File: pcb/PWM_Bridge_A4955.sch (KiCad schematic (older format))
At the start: 18 parts, among them Q3 IPD079N06L3G, Q4 IPD079N06L3G, Q5 IPD079N06L3G, Q6 IPD079N06L3G, U5 A4955GLPTR-T

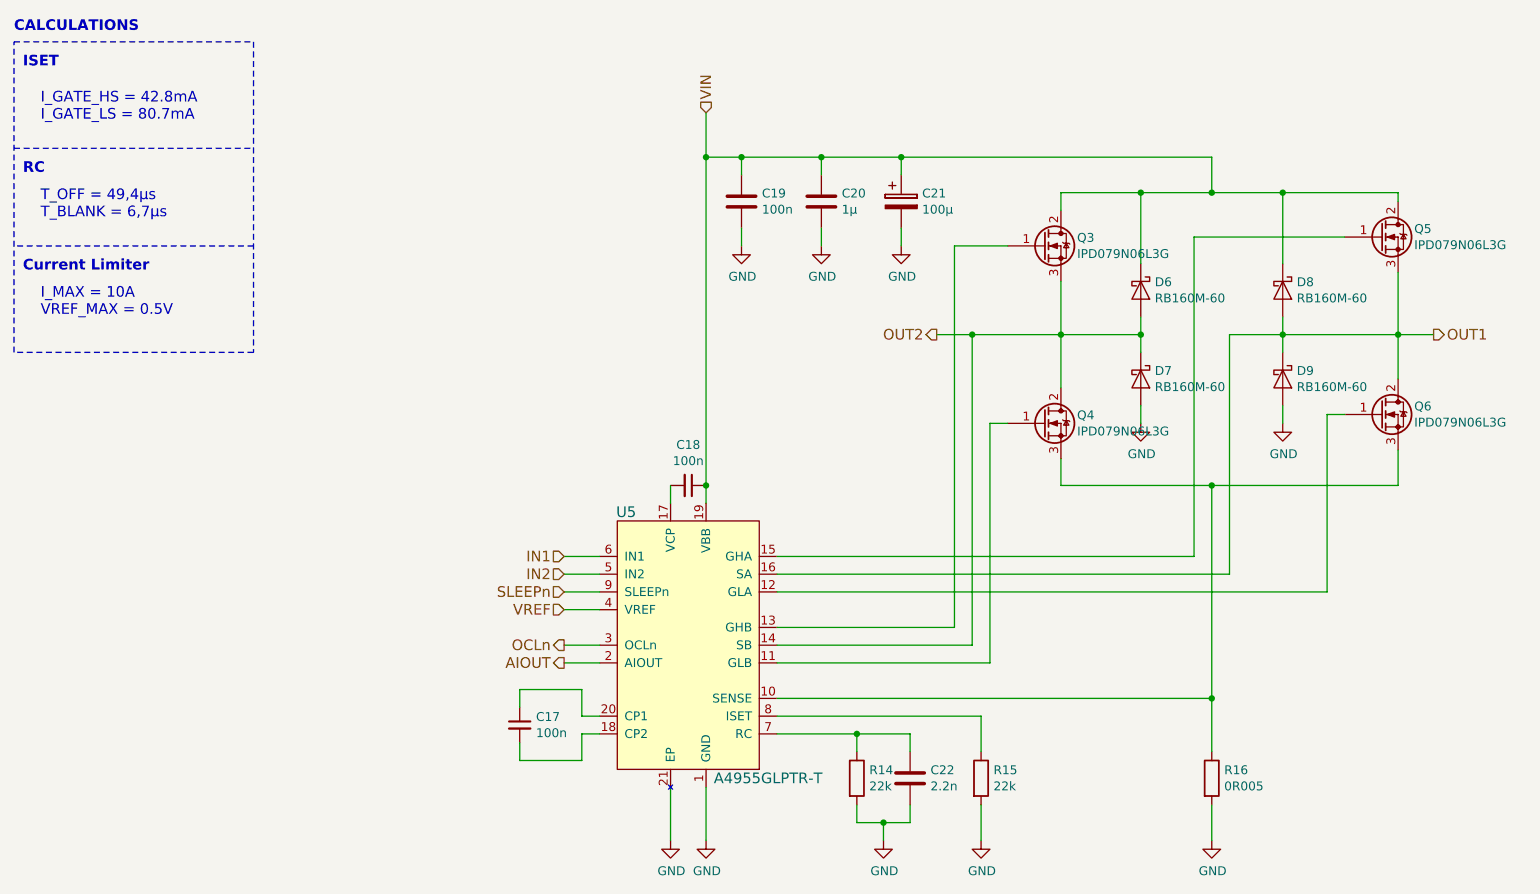
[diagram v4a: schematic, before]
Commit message: Fix schematic error described in #8
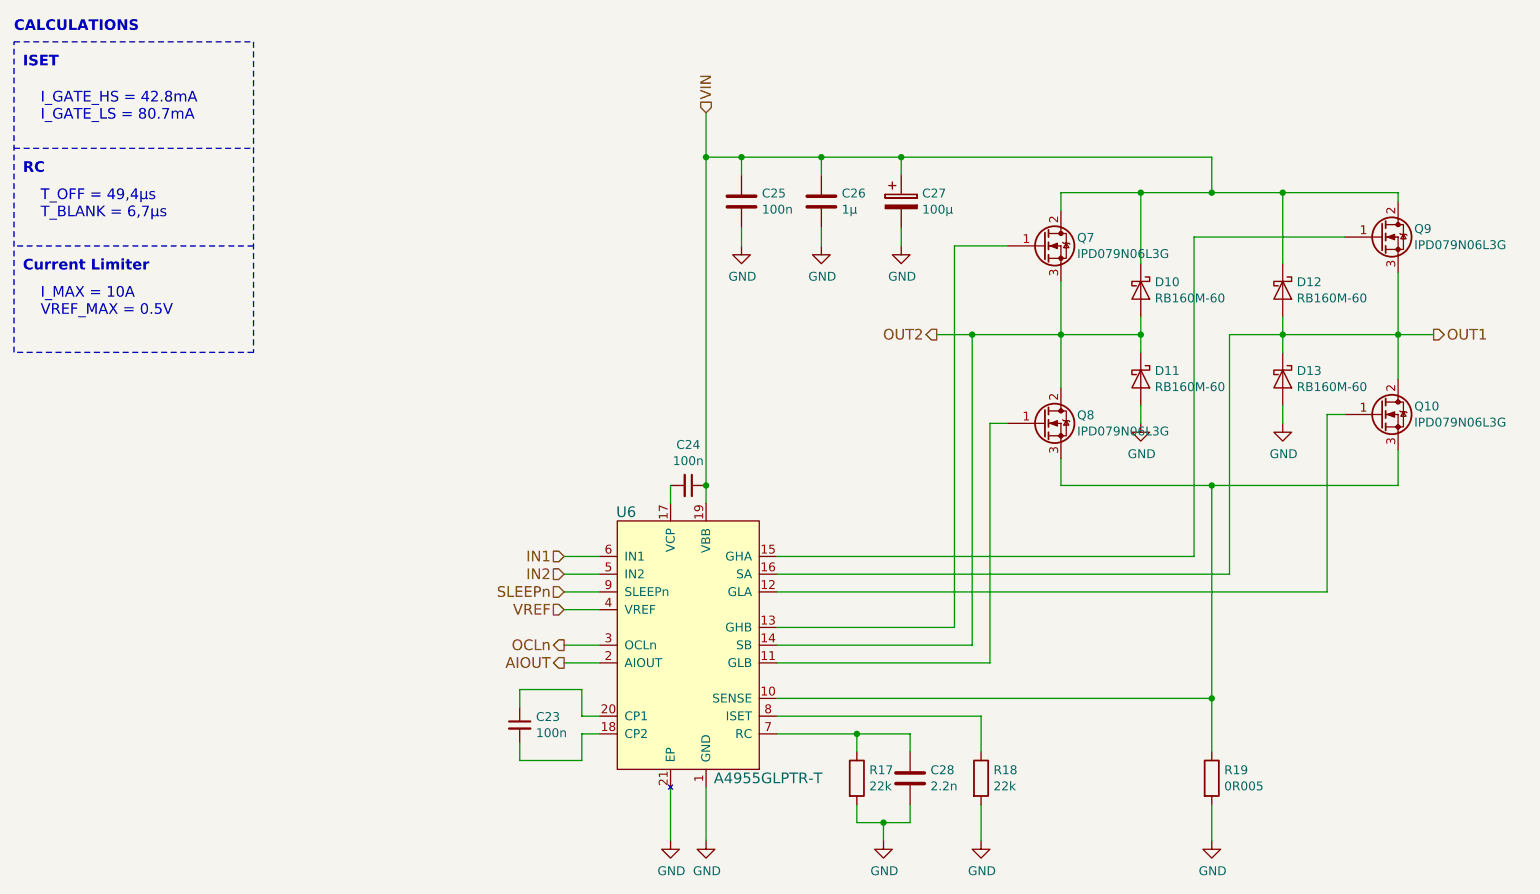
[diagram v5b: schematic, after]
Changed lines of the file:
@@
 $Descr A4 11693 8268
 encoding utf-8
-Sheet 3 7
+Sheet 4 7
 Title "A4955 PWM Bridge"
 Date "2016-12-03"
@@
 AR Path="/58077727/58077F1C" Ref="U5"  Part="1"
 AR Path="/58084D17/58077F1C" Ref="U6"  Part="1"
-F 0 "U5" H 4300 5150 60  0000 C CNN
+F 0 "U6" H 4300 5150 60  0000 C CNN
 F 1 "A4955GLPTR-T" H 5100 3650 60  0000 C CNN
 F 2 "Housings_SSOP:ETSSOP-20-1EP_4.4x6.5mm_Pitch0.65mm" H 4650 4400 60  0001 C CNN
@@
 AR Path="/58077727/5807829A" Ref="C18"  Part="1"
 AR Path="/58084D17/5807829A" Ref="C24"  Part="1"
-F 0 "C18" V 4421 3500 50  0000 C CNN
+F 0 "C24" V 4421 3500 50  0000 C CNN
 F 1 "100n" V 4512 3500 50  0000 C CNN
 F 2 "Capacitors_SMD:C_0603" H 4650 3500 50  0001 C CNN
@@
 AR Path="/58077727/58078520" Ref="R14"  Part="1"
 AR Path="/58084D17/58078520" Ref="R17"  Part="1"
-F 0 "R14" H 5670 5196 50  0000 L CNN
+F 0 "R17" H 5670 5196 50  0000 L CNN
 F 1 "22k" H 5670 5105 50  0000 L CNN
 F 2 "Resistors_SMD:R_0603" V 5530 5150 50  0001 C CNN
@@
 AR Path="/58077727/5807867B" Ref="C22"  Part="1"
 AR Path="/58084D17/5807867B" Ref="C28"  Part="1"
-F 0 "C22" H 6015 5196 50  0000 L CNN
+F 0 "C28" H 6015 5196 50  0000 L CNN
 F 1 "2.2n" H 6015 5105 50  0000 L CNN
 F 2 "Capacitors_SMD:C_0603" H 5938 5000 50  0001 C CNN
@@
 $EndComp
 $Comp
-L GND #PWR073
+L GND #PWR072
 U 1 1 580787DB
 P 5750 5500
-AR Path="/58077727/580787DB" Ref="#PWR073"  Part="1"
-AR Path="/58084D17/580787DB" Ref="#PWR083"  Part="1"
-F 0 "#PWR073" H 5750 5250 50  0001 C CNN
+AR Path="/58077727/580787DB" Ref="#PWR072"  Part="1"
+AR Path="/58084D17/580787DB" Ref="#PWR082"  Part="1"
+F 0 "#PWR082" H 5750 5250 50  0001 C CNN
 F 1 "GND" H 5755 5327 50  0000 C CNN
 F 2 "" H 5750 5500 50  0000 C CNN
@@
 $EndComp
 $Comp
-L GND #PWR074
+L GND #PWR073
 U 1 1 58078835
 P 4750 5500
-AR Path="/58077727/58078835" Ref="#PWR074"  Part="1"
-AR Path="/58084D17/58078835" Ref="#PWR084"  Part="1"
-F 0 "#PWR074" H 4750 5250 50  0001 C CNN
+AR Path="/58077727/58078835" Ref="#PWR073"  Part="1"
+AR Path="/58084D17/58078835" Ref="#PWR083"  Part="1"
+F 0 "#PWR083" H 4750 5250 50  0001 C CNN
 F 1 "GND" H 4755 5327 50  0000 C CNN
 F 2 "" H 4750 5500 50  0000 C CNN
@@
 AR Path="/58077727/580789CE" Ref="R16"  Part="1"
 AR Path="/58084D17/580789CE" Ref="R19"  Part="1"
-F 0 "R16" H 7670 5196 50  0000 L CNN
+F 0 "R19" H 7670 5196 50  0000 L CNN
 F 1 "0R005" H 7670 5105 50  0000 L CNN
 F 2 "Resistors_SMD:R_2512" V 7530 5150 50  0001 C CNN
@@
 $EndComp
 $Comp
-L GND #PWR075
+L GND #PWR074
 U 1 1 58078AB1
 P 7600 5500
-AR Path="/58077727/58078AB1" Ref="#PWR075"  Part="1"
-AR Path="/58084D17/58078AB1" Ref="#PWR085"  Part="1"
-F 0 "#PWR075" H 7600 5250 50  0001 C CNN
+AR Path="/58077727/58078AB1" Ref="#PWR074"  Part="1"
+AR Path="/58084D17/58078AB1" Ref="#PWR084"  Part="1"
+F 0 "#PWR084" H 7600 5250 50  0001 C CNN
 F 1 "GND" H 7605 5327 50  0000 C CNN
 F 2 "" H 7600 5500 50  0000 C CNN
@@
 AR Path="/58077727/58078C46" Ref="Q3"  Part="1"
 AR Path="/58084D17/58078C46" Ref="Q7"  Part="1"
-F 0 "Q3" H 6841 2196 50  0000 L CNN
+F 0 "Q7" H 6841 2196 50  0000 L CNN
 F 1 "IPD079N06L3G" H 6841 2105 50  0000 L CNN
 F 2 "TO_SOT_Packages_SMD_local:PG-TO-252-3-313" H 6850 2250 50  0001 C CNN
@@
 AR Path="/58077727/58078E80" Ref="Q5"  Part="1"
 AR Path="/58084D17/58078E80" Ref="Q9"  Part="1"
-F 0 "Q5" H 8741 2146 50  0000 L CNN
+F 0 "Q9" H 8741 2146 50  0000 L CNN
 F 1 "IPD079N06L3G" H 8741 2055 50  0000 L CNN
 F 2 "TO_SOT_Packages_SMD_local:PG-TO-252-3-313" H 8750 2200 50  0001 C CNN
@@
 AR Path="/58077727/58078ED9" Ref="Q6"  Part="1"
 AR Path="/58084D17/58078ED9" Ref="Q10"  Part="1"
-F 0 "Q6" H 8741 3146 50  0000 L CNN
+F 0 "Q10" H 8741 3146 50  0000 L CNN
 F 1 "IPD079N06L3G" H 8741 3055 50  0000 L CNN
 F 2 "TO_SOT_Packages_SMD_local:PG-TO-252-3-313" H 8750 3200 50  0001 C CNN
@@
 AR Path="/58077727/58078F3F" Ref="Q4"  Part="1"
 AR Path="/58084D17/58078F3F" Ref="Q8"  Part="1"
-F 0 "Q4" H 6841 3196 50  0000 L CNN
+F 0 "Q8" H 6841 3196 50  0000 L CNN
 F 1 "IPD079N06L3G" H 6841 3105 50  0000 L CNN
 F 2 "TO_SOT_Packages_SMD_local:PG-TO-252-3-313" H 6850 3250 50  0001 C CNN
@@
 AR Path="/58077727/5807A394" Ref="C19"  Part="1"
 AR Path="/58084D17/5807A394" Ref="C25"  Part="1"
-F 0 "C19" H 5065 1946 50  0000 L CNN
+F 0 "C25" H 5065 1946 50  0000 L CNN
 F 1 "100n" H 5065 1855 50  0000 L CNN
 F 2 "Capacitors_SMD:C_0603" H 4988 1750 50  0001 C CNN
@@
 $EndComp
 $Comp
-L GND #PWR076
+L GND #PWR075
 U 1 1 5807A4C6
 P 4950 2150
-AR Path="/58077727/5807A4C6" Ref="#PWR076"  Part="1"
-AR Path="/58084D17/5807A4C6" Ref="#PWR086"  Part="1"
-F 0 "#PWR076" H 4950 1900 50  0001 C CNN
+AR Path="/58077727/5807A4C6" Ref="#PWR075"  Part="1"
+AR Path="/58084D17/5807A4C6" Ref="#PWR085"  Part="1"
+F 0 "#PWR085" H 4950 1900 50  0001 C CNN
 F 1 "GND" H 4955 1977 50  0000 C CNN
 F 2 "" H 4950 2150 50  0000 C CNN
@@
 AR Path="/58077727/5807A62E" Ref="C21"  Part="1"
 AR Path="/58084D17/5807A62E" Ref="C27"  Part="1"
-F 0 "C21" H 5968 1946 50  0000 L CNN
+F 0 "C27" H 5968 1946 50  0000 L CNN
 F 1 "100µ" H 5968 1855 50  0000 L CNN
 F 2 "Capacitors_SMD:c_elec_10x10" H 5888 1750 50  0001 C CNN
@@
 $EndComp
 $Comp
-L GND #PWR077
+L GND #PWR076
 U 1 1 5807A964
 P 5850 2150
-AR Path="/58077727/5807A964" Ref="#PWR077"  Part="1"
-AR Path="/58084D17/5807A964" Ref="#PWR087"  Part="1"
-F 0 "#PWR077" H 5850 1900 50  0001 C CNN
+AR Path="/58077727/5807A964" Ref="#PWR076"  Part="1"
+AR Path="/58084D17/5807A964" Ref="#PWR086"  Part="1"
+F 0 "#PWR086" H 5850 1900 50  0001 C CNN
 F 1 "GND" H 5855 1977 50  0000 C CNN
 F 2 "" H 5850 2150 50  0000 C CNN
@@
 AR Path="/58077727/5807BEA4" Ref="C17"  Part="1"
 AR Path="/58084D17/5807BEA4" Ref="C23"  Part="1"
-F 0 "C17" H 3792 4896 50  0000 L CNN
+F 0 "C23" H 3792 4896 50  0000 L CNN
 F 1 "100n" H 3792 4805 50  0000 L CNN
 F 2 "Capacitors_SMD:C_0603" H 3700 4850 50  0001 C CNN
@@
 AR Path="/58077727/5809AC71" Ref="C20"  Part="1"
 AR Path="/58084D17/5809AC71" Ref="C26"  Part="1"
-F 0 "C20" H 5515 1946 50  0000 L CNN
+F 0 "C26" H 5515 1946 50  0000 L CNN
 F 1 "1µ" H 5515 1855 50  0000 L CNN
 F 2 "Capacitors_SMD:C_0603" H 5438 1750 50  0001 C CNN
@@
 $EndComp
 $Comp
-L GND #PWR088
+L GND #PWR087
 U 1 1 5809ACB6
 P 5400 2150
-AR Path="/58084D17/5809ACB6" Ref="#PWR088"  Part="1"
-AR Path="/58077727/5809ACB6" Ref="#PWR078"  Part="1"
-F 0 "#PWR078" H 5400 1900 50  0001 C CNN
+AR Path="/58084D17/5809ACB6" Ref="#PWR087"  Part="1"
+AR Path="/58077727/5809ACB6" Ref="#PWR077"  Part="1"
+F 0 "#PWR087" H 5400 1900 50  0001 C CNN
 F 1 "GND" H 5405 1977 50  0000 C CNN
 F 2 "" H 5400 2150 50  0000 C CNN
@@
 AR Path="/58077727/580A461C" Ref="R15"  Part="1"
 AR Path="/58084D17/580A461C" Ref="R18"  Part="1"
-F 0 "R15" H 6370 5196 50  0000 L CNN
+F 0 "R18" H 6370 5196 50  0000 L CNN
 F 1 "22k" H 6370 5105 50  0000 L CNN
 F 2 "Resistors_SMD:R_0603" V 6230 5150 50  0001 C CNN
@@
 $EndComp
 $Comp
-L GND #PWR079
+L GND #PWR078
 U 1 1 580A46B3
 P 6300 5500
-AR Path="/58077727/580A46B3" Ref="#PWR079"  Part="1"
-AR Path="/58084D17/580A46B3" Ref="#PWR089"  Part="1"
-F 0 "#PWR079" H 6300 5250 50  0001 C CNN
+AR Path="/58077727/580A46B3" Ref="#PWR078"  Part="1"
+AR Path="/58084D17/580A46B3" Ref="#PWR088"  Part="1"
+F 0 "#PWR088" H 6300 5250 50  0001 C CNN
 F 1 "GND" H 6305 5327 50  0000 C CNN
 F 2 "" H 6300 5500 50  0000 C CNN
@@
 $EndComp
 $Comp
-L GND #PWR080
+L GND #PWR079
 U 1 1 581550B7
 P 8000 3150
-AR Path="/58077727/581550B7" Ref="#PWR080"  Part="1"
-AR Path="/58084D17/581550B7" Ref="#PWR090"  Part="1"
-F 0 "#PWR080" H 8000 2900 50  0001 C CNN
+AR Path="/58077727/581550B7" Ref="#PWR079"  Part="1"
+AR Path="/58084D17/581550B7" Ref="#PWR089"  Part="1"
+F 0 "#PWR089" H 8000 2900 50  0001 C CNN
 F 1 "GND" H 8005 2977 50  0000 C CNN
 F 2 "" H 8000 3150 50  0000 C CNN
@@
 $EndComp
 $Comp
-L GND #PWR081
+L GND #PWR080
 U 1 1 58155164
 P 7200 3150
-AR Path="/58077727/58155164" Ref="#PWR081"  Part="1"
-AR Path="/58084D17/58155164" Ref="#PWR091"  Part="1"
-F 0 "#PWR081" H 7200 2900 50  0001 C CNN
+AR Path="/58077727/58155164" Ref="#PWR080"  Part="1"
+AR Path="/58084D17/58155164" Ref="#PWR090"  Part="1"
+F 0 "#PWR090" H 7200 2900 50  0001 C CNN
 F 1 "GND" H 7205 2977 50  0000 C CNN
 F 2 "" H 7200 3150 50  0000 C CNN
@@
 	850  2750 850  1000
 $Comp
-L GND #PWR082
+L GND #PWR081
 U 1 1 582EE915
 P 4550 5500
-AR Path="/58077727/582EE915" Ref="#PWR082"  Part="1"
-AR Path="/58084D17/582EE915" Ref="#PWR092"  Part="1"
-F 0 "#PWR082" H 4550 5250 50  0001 C CNN
+AR Path="/58077727/582EE915" Ref="#PWR081"  Part="1"
+AR Path="/58084D17/582EE915" Ref="#PWR091"  Part="1"
+F 0 "#PWR091" H 4550 5250 50  0001 C CNN
 F 1 "GND" H 4555 5327 50  0000 C CNN
 F 2 "" H 4550 5500 50  0000 C CNN
@@
 AR Path="/58077727/5849BEDB" Ref="D6"  Part="1"
 AR Path="/58084D17/5849BEDB" Ref="D10"  Part="1"
-F 0 "D6" V 7154 2479 50  0000 L CNN
+F 0 "D10" V 7154 2479 50  0000 L CNN
 F 1 "RB160M-60" V 7245 2479 50  0000 L CNN
 F 2 "Diodes_SMD:SOD-123" V 7291 2479 50  0001 L CNN
@@
 AR Path="/58077727/5849C456" Ref="D7"  Part="1"
 AR Path="/58084D17/5849C456" Ref="D11"  Part="1"
-F 0 "D7" V 7154 2979 50  0000 L CNN
+F 0 "D11" V 7154 2979 50  0000 L CNN
 F 1 "RB160M-60" V 7245 2979 50  0000 L CNN
 F 2 "Diodes_SMD:SOD-123" V 7291 2979 50  0001 L CNN
@@
 AR Path="/58084D17/5849D384" Ref="D12"  Part="1"
 AR Path="/58077727/5849D384" Ref="D8"  Part="1"
-F 0 "D8" V 7954 2479 50  0000 L CNN
+F 0 "D12" V 7954 2479 50  0000 L CNN
 F 1 "RB160M-60" V 8045 2479 50  0000 L CNN
 F 2 "Diodes_SMD:SOD-123" V 8091 2479 50  0001 L CNN
@@
 AR Path="/58084D17/5849D3E7" Ref="D13"  Part="1"
 AR Path="/58077727/5849D3E7" Ref="D9"  Part="1"
-F 0 "D9" V 7954 2979 50  0000 L CNN
+F 0 "D13" V 7954 2979 50  0000 L CNN
 F 1 "RB160M-60" V 8045 2979 50  0000 L CNN
 F 2 "Diodes_SMD:SOD-123" V 8091 2979 50  0001 L CNN

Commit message: Little update
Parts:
- C20: Digi-Key Part Number 311-1343-1-ND -> 311-1787-1-ND
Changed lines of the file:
@@
 F 2 "Capacitors_SMD:C_0603" H 5438 1750 50  0001 C CNN
 F 3 "" H 5400 1900 50  0000 C CNN
-F 4 "311-1343-1-ND" H 5400 1900 60  0001 C CNN "Digi-Key Part Number"
+F 4 "311-1787-1-ND" H 5400 1900 60  0001 C CNN "Digi-Key Part Number"
 F 5 "1" H 5400 1900 60  0001 C CNN "Digi-Key Minimum Quantity"
 	1    5400 1900
